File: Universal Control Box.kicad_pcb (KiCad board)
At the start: 2 copper layers, 169.7 x 93.2 mm, 84 parts, among them J101 Conn_01x06, J102 Conn_01x07, J103 USB_C_Receptacle_USB2.0, U101 ESP32-WROOM-32, U102 PCF8575DBR (PCF1), U103 AMS1117-3.3, U201 PEC11H-4025F-S0016, U202 PEC11H-4025F-S0016

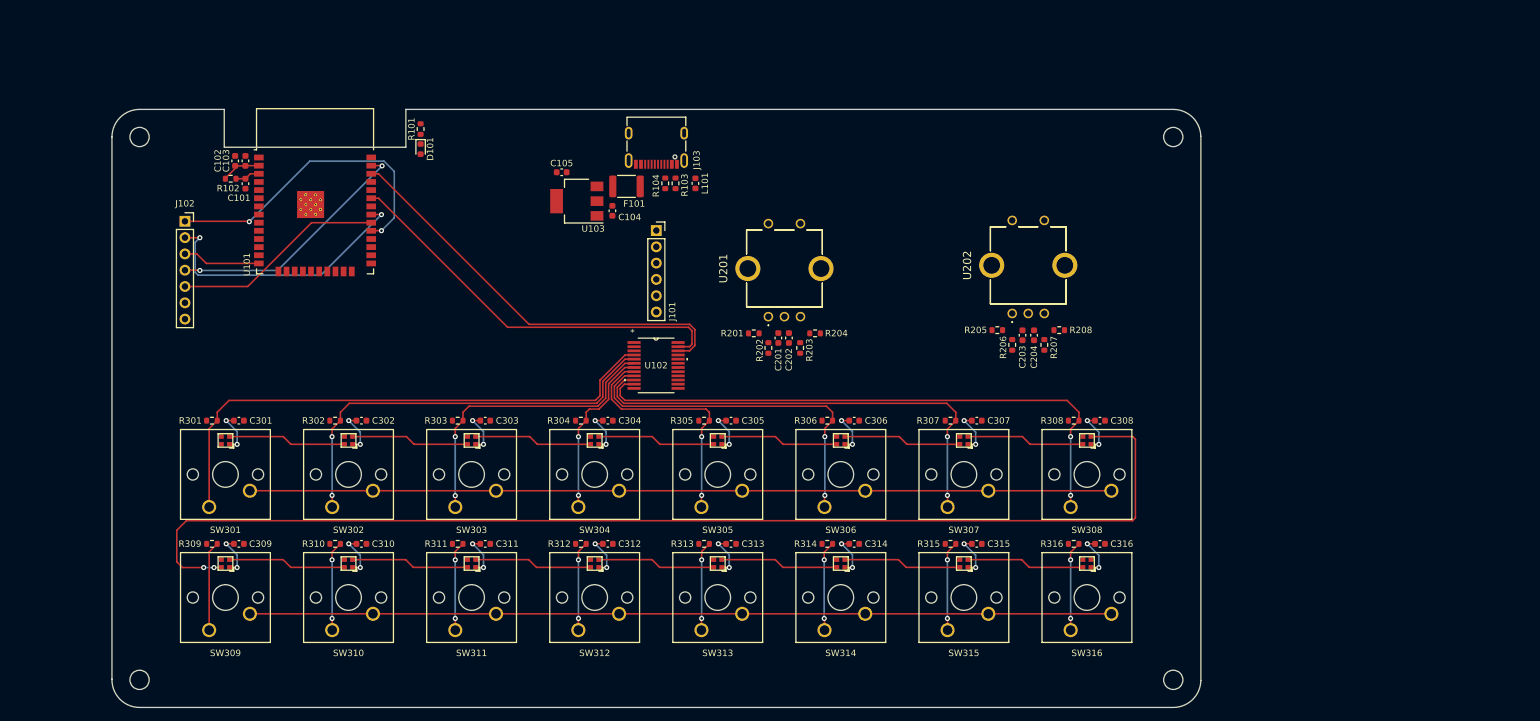
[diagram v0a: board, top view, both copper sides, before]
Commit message: Fixed LED Schematic & added 2 more LEDs
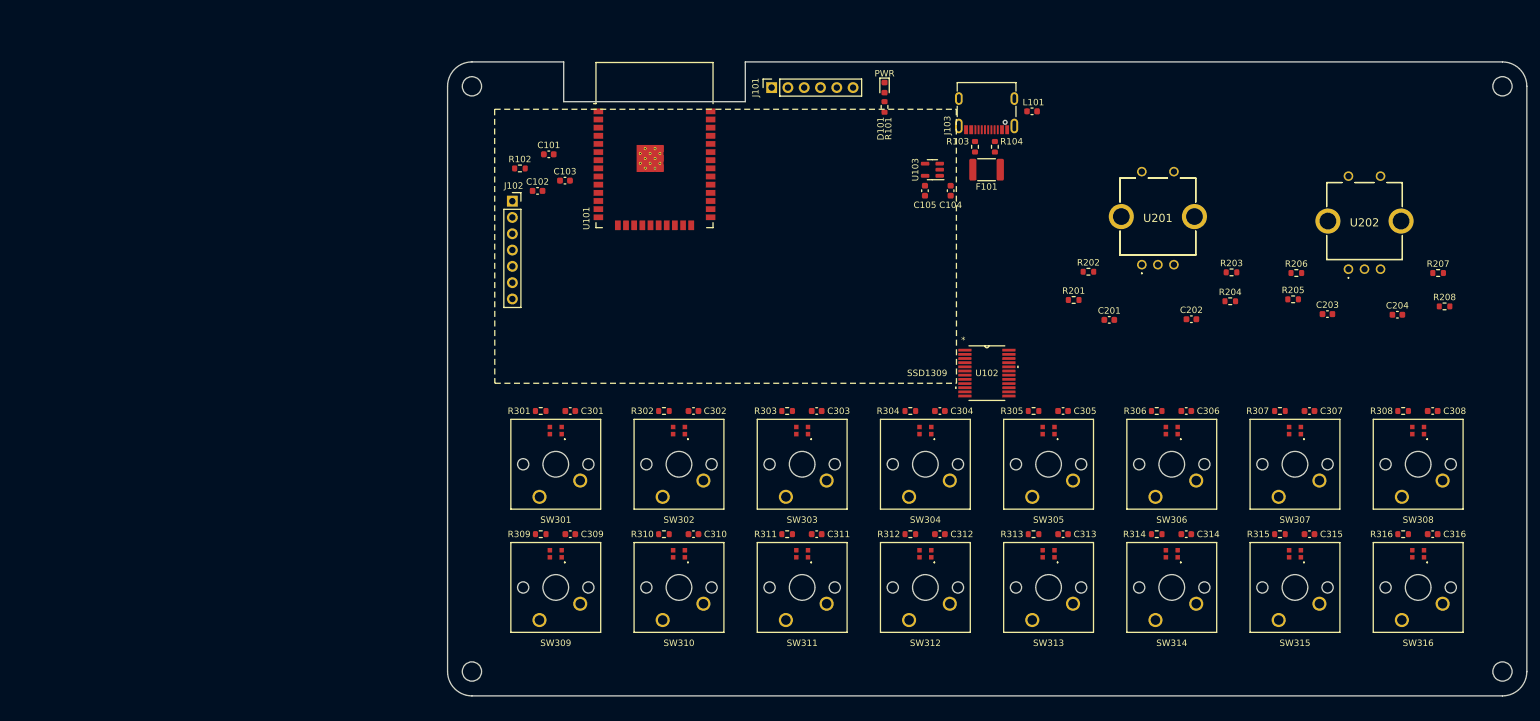
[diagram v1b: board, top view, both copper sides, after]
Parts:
- C104: value 10uF -> 22uF
- C105: value 10uF -> 4.7uF
- SW301, SW302, SW303, SW304, SW305, SW306, SW307, SW308, SW309, SW310, SW311, SW312, SW313, SW314, SW315, SW316: footprint Adam_Custom_Footprints:CherryMX_1.00u_PCB_SK6812-EC20 -> Adam_Custom_Footprints:CherryMX_1.00u_PCB_WS2812B-2020
- U103: value AMS1117-3.3 -> XC6220B331MR-G; footprint Package_TO_SOT_SMD:SOT-223-3_TabPin2 -> Package_TO_SOT_SMD:SOT-23-5
- moved H102 231.7 mm to (247.1, 30.7)
- moved H103 137.4 mm to (86.5, 121.9)
- moved D101 72.9 mm to (150.8, 30.9)
- moved R101 72.4 mm to (150.8, 33.9), turned to -90 degrees
- moved R203 68.2 mm to (204.9, 59.7), turned to 0 degrees
- moved R204 64.9 mm to (204.7, 64.2), turned to 0 degrees
- moved C202 62.8 mm to (198.6, 67.0), turned to 0 degrees
- moved R207 62.4 mm to (237.1, 59.8), turned to 0 degrees
- moved R208 60.2 mm to (238.1, 65.0), turned to 0 degrees
- moved U201 58.8 mm to (190.9, 58.5)
- moved C204 56.7 mm to (230.7, 66.3), turned to 0 degrees
- moved C105 56.7 mm to (157.1, 47.0), turned to -90 degrees
- moved F101 56.2 mm to (166.7, 43.7)
- moved U103 55.6 mm to (158.3, 43.7)
- moved L101 53.6 mm to (173.8, 34.6), turned to 180 degrees
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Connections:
- net /OLED_CLK renamed /OLED_SCL
- net /OLED_MOSI_SDA renamed /OLED_MOSI
- C104 pad 1: +5V -> GND
- C104 pad 2: GND -> +5V
- J102 pad 2: /OLED_MISO_SCK -> /OLED_DC
- SW301 pad 2: +5V -> /KeyCaps/SW1
- SW301 pad 3: Net-(SW301-DOUT) -> +5V
- SW301 pad 4: /KeyCaps/SW1 -> Net-(SW301-DOUT)
- SW302 pad 2: +5V -> /KeyCaps/SW2
- SW302 pad 3: Net-(SW302-DOUT) -> +5V
- SW302 pad 4: /KeyCaps/SW2 -> Net-(SW302-DOUT)
- SW303 pad 2: +5V -> /KeyCaps/SW3
- SW303 pad 3: Net-(SW303-DOUT) -> +5V
- SW303 pad 4: /KeyCaps/SW3 -> Net-(SW303-DOUT)
- SW304 pad 2: +5V -> /KeyCaps/SW4
- SW304 pad 3: Net-(SW304-DOUT) -> +5V
- SW304 pad 4: /KeyCaps/SW4 -> Net-(SW304-DOUT)
- SW305 pad 2: +5V -> /KeyCaps/SW5
- SW305 pad 3: Net-(SW305-DOUT) -> +5V
- SW305 pad 4: /KeyCaps/SW5 -> Net-(SW305-DOUT)
- SW306 pad 2: +5V -> /KeyCaps/SW6
- SW306 pad 3: Net-(SW306-DOUT) -> +5V
- SW306 pad 4: /KeyCaps/SW6 -> Net-(SW306-DOUT)
- SW307 pad 2: +5V -> /KeyCaps/SW7
- SW307 pad 3: Net-(SW307-DOUT) -> +5V
- SW307 pad 4: /KeyCaps/SW7 -> Net-(SW307-DOUT)
- SW308 pad 2: +5V -> /KeyCaps/SW8
- SW308 pad 3: Net-(SW308-DOUT) -> +5V
- SW308 pad 4: /KeyCaps/SW8 -> Net-(SW308-DOUT)
- SW309 pad 2: +5V -> /KeyCaps/SW9
- SW309 pad 3: Net-(SW309-DOUT) -> +5V
- SW309 pad 4: /KeyCaps/SW9 -> Net-(SW309-DOUT)
- SW310 pad 2: +5V -> /KeyCaps/SW10
- SW310 pad 3: Net-(SW310-DOUT) -> +5V
- SW310 pad 4: /KeyCaps/SW10 -> Net-(SW310-DOUT)
- SW311 pad 2: +5V -> /KeyCaps/SW11
- SW311 pad 3: Net-(SW311-DOUT) -> +5V
- SW311 pad 4: /KeyCaps/SW11 -> Net-(SW311-DOUT)
- SW312 pad 2: +5V -> /KeyCaps/SW12
- SW312 pad 3: Net-(SW312-DOUT) -> +5V
- SW312 pad 4: /KeyCaps/SW12 -> Net-(SW312-DOUT)
- SW313 pad 2: +5V -> /KeyCaps/SW13
- SW313 pad 3: Net-(SW313-DOUT) -> +5V
- SW313 pad 4: /KeyCaps/SW13 -> Net-(SW313-DOUT)
- SW314 pad 2: +5V -> /KeyCaps/SW14
- SW314 pad 3: Net-(SW314-DOUT) -> +5V
- SW314 pad 4: /KeyCaps/SW14 -> Net-(SW314-DOUT)
- SW315 pad 2: +5V -> /KeyCaps/SW15
- SW315 pad 3: Net-(SW315-DOUT) -> +5V
- SW315 pad 4: /KeyCaps/SW15 -> Net-(SW315-DOUT)
- SW316 pad 2: +5V -> /KeyCaps/SW16
- SW316 pad 3: unconnected-(SW316-DOUT-Pad3) -> +5V
- SW316 pad 4: /KeyCaps/SW16 -> unconnected-(SW316-DOUT-Pad4)
- U101 pad 14: /OLED_RESET -> unconnected-(U101-IO12-Pad14)
- U101 pad 31: /OLED_MISO_SCK -> /IO_INT
- U101 pad 8: unconnected-(U101-IO32-Pad8) -> /OLED_RESET
- U101 pad 9: unconnected-(U101-IO33-Pad9) -> /OLED_DC
- U102 pad 1: unconnected-(U102-*INT-Pad1) -> /IO_INT
- U102 pad 10: /KeyCaps/SW7 -> /KeyCaps/SW10
- U102 pad 11: /KeyCaps/SW8 -> /KeyCaps/SW9
- U102 pad 17: /KeyCaps/SW12 -> /KeyCaps/SW5
- U102 pad 18: /KeyCaps/SW11 -> /KeyCaps/SW6
- U102 pad 19: /KeyCaps/SW10 -> /KeyCaps/SW7
- U102 pad 20: /KeyCaps/SW9 -> /KeyCaps/SW8
- U102 pad 8: /KeyCaps/SW5 -> /KeyCaps/SW12
- U102 pad 9: /KeyCaps/SW6 -> /KeyCaps/SW11
- U103 pad 1: GND -> +5V
- U103 pad 2: +3.3V -> GND
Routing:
- net +3.3V: track 274.9 -> 0.00 mm
- net Net-(SW308-DOUT): track 181.8 -> 0.00 mm, vias 2 -> 0
- net +5V: track 109.1 -> 0.00 mm, vias 32 -> 0
- net /KeyCaps/SW8: track 91.4 -> 0.00 mm, vias 2 -> 0
- net /KeyCaps/SW1: track 85.4 -> 0.00 mm
- net /KeyCaps/SW7: track 73.6 -> 0.00 mm, vias 2 -> 0
- net /KeyCaps/SW2: track 66.0 -> 0.00 mm, vias 2 -> 0
- net /I2C_SCL: track 65.9 -> 0.00 mm
- net /I2C_SDA: track 63.0 -> 0.00 mm
- net /KeyCaps/SW6: track 55.8 -> 0.00 mm, vias 2 -> 0
- net /OLED_CS: track 48.9 -> 0.00 mm, vias 2 -> 0
- net /KeyCaps/SW3: track 46.5 -> 0.00 mm, vias 2 -> 0
- net /OLED_MISO_SCK: track 42.7 -> 0.00 mm, vias 2 -> 0
- net /OLED_MOSI: track 39.2 -> 0.00 mm, vias 2 -> 0
- net /KeyCaps/SW5: track 38.0 -> 0.00 mm, vias 2 -> 0
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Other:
- board size 169.7 x 93.2 mm -> 168.2 x 98.8 mm
- board text added: "PWR"

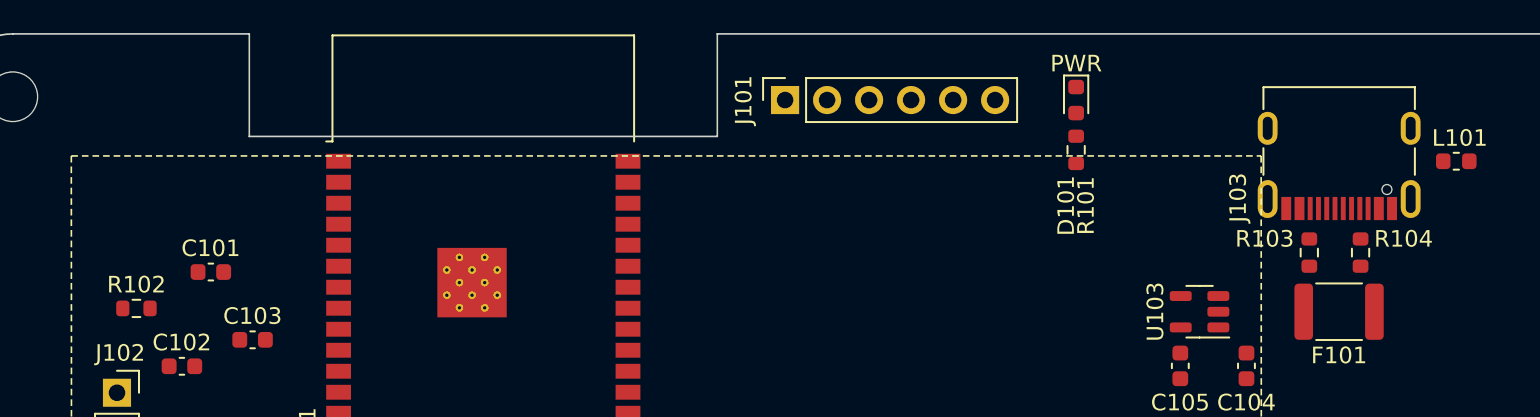
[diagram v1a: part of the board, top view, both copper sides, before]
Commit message: Added missing resistor for Green LED
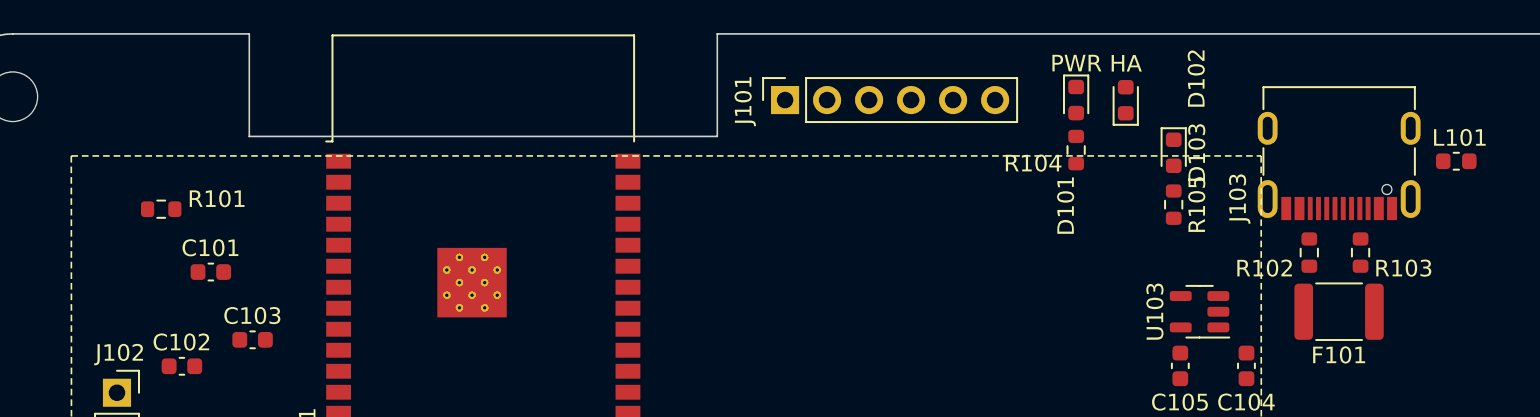
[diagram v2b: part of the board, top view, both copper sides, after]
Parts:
- added D102: Green, LED_SMD:LED_0603_1608Metric, F.Cu at (153.8, 30.9)
- added D103: Yellow, LED_SMD:LED_0603_1608Metric, F.Cu at (156.7, 34.1)
- added R105: 1K, Resistor_SMD:R_0603_1608Metric, F.Cu at (156.7, 37.2)
- R101: value 1K -> 10K
- R102: value 10K -> 5.1K
- R104: value 5.1K -> 1K
- moved R102 71.0 mm to (164.9, 40.1), turned to -90 degrees
- moved R101 55.4 mm to (95.5, 37.5), turned to 0 degrees
- moved R104 18.3 mm to (150.8, 33.9), turned to -90 degrees
- moved R103 3.10 mm to (168.0, 40.1), turned to 90 degrees
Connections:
- D101 pad 1: Net-(D101-K) -> GND
- D101 pad 2: +3.3V -> Net-(D101-A)
- R101 pad 1: Net-(D101-K) -> +3.3V
- R101 pad 2: GND -> /EN
- R102 pad 1: +3.3V -> Net-(J103-CC2)
- R102 pad 2: /EN -> GND
- R103 pad 1: Net-(J103-CC2) -> GND
- R103 pad 2: GND -> Net-(J103-CC1)
- R104 pad 1: GND -> Net-(D101-A)
- R104 pad 2: Net-(J103-CC1) -> +3.3V
- R302 pad 1: /KeyCaps/SW2 -> /KeyCaps/SW9
- R303 pad 1: /KeyCaps/SW3 -> /KeyCaps/SW2
- R304 pad 1: /KeyCaps/SW4 -> /KeyCaps/SW10
- R305 pad 1: /KeyCaps/SW5 -> /KeyCaps/SW3
- R306 pad 1: /KeyCaps/SW6 -> /KeyCaps/SW11
- R307 pad 1: /KeyCaps/SW7 -> /KeyCaps/SW4
- R308 pad 1: /KeyCaps/SW8 -> /KeyCaps/SW12
- R309 pad 1: /KeyCaps/SW9 -> /KeyCaps/SW5
- R310 pad 1: /KeyCaps/SW10 -> /KeyCaps/SW13
- R311 pad 1: /KeyCaps/SW11 -> /KeyCaps/SW6
- R312 pad 1: /KeyCaps/SW12 -> /KeyCaps/SW14
- R313 pad 1: /KeyCaps/SW13 -> /KeyCaps/SW7
- R314 pad 1: /KeyCaps/SW14 -> /KeyCaps/SW15
- R315 pad 1: /KeyCaps/SW15 -> /KeyCaps/SW8
- SW302 pad 2: /KeyCaps/SW2 -> /KeyCaps/SW9
- SW302 pad 5: Net-(SW301-DOUT) -> Net-(SW302-DIN)
- SW303 pad 2: /KeyCaps/SW3 -> /KeyCaps/SW2
- SW303 pad 5: Net-(SW302-DOUT) -> Net-(SW301-DOUT)
- SW304 pad 2: /KeyCaps/SW4 -> /KeyCaps/SW10
- SW304 pad 5: Net-(SW303-DOUT) -> Net-(SW302-DOUT)
- SW305 pad 2: /KeyCaps/SW5 -> /KeyCaps/SW3
- SW305 pad 5: Net-(SW304-DOUT) -> Net-(SW303-DOUT)
- SW306 pad 2: /KeyCaps/SW6 -> /KeyCaps/SW11
- SW306 pad 5: Net-(SW305-DOUT) -> Net-(SW304-DOUT)
- SW307 pad 2: /KeyCaps/SW7 -> /KeyCaps/SW4
- SW307 pad 5: Net-(SW306-DOUT) -> Net-(SW305-DOUT)
- SW308 pad 2: /KeyCaps/SW8 -> /KeyCaps/SW12
- SW308 pad 5: Net-(SW307-DOUT) -> Net-(SW306-DOUT)
- SW309 pad 2: /KeyCaps/SW9 -> /KeyCaps/SW5
- SW309 pad 5: Net-(SW308-DOUT) -> Net-(SW307-DOUT)
- SW310 pad 2: /KeyCaps/SW10 -> /KeyCaps/SW13
- SW310 pad 5: Net-(SW309-DOUT) -> Net-(SW308-DOUT)
- SW311 pad 2: /KeyCaps/SW11 -> /KeyCaps/SW6
- SW311 pad 5: Net-(SW310-DOUT) -> Net-(SW309-DOUT)
- SW312 pad 2: /KeyCaps/SW12 -> /KeyCaps/SW14
- SW312 pad 5: Net-(SW311-DOUT) -> Net-(SW310-DOUT)
- SW313 pad 2: /KeyCaps/SW13 -> /KeyCaps/SW7
- SW313 pad 5: Net-(SW312-DOUT) -> Net-(SW311-DOUT)
- SW314 pad 2: /KeyCaps/SW14 -> /KeyCaps/SW15
- SW314 pad 5: Net-(SW313-DOUT) -> Net-(SW312-DOUT)
- SW315 pad 2: /KeyCaps/SW15 -> /KeyCaps/SW8
- SW315 pad 4: Net-(SW315-DOUT) -> Net-(SW302-DIN)
- SW315 pad 5: Net-(SW314-DOUT) -> Net-(SW313-DOUT)
- SW316 pad 5: Net-(SW315-DOUT) -> Net-(SW314-DOUT)
- U101 pad 23: unconnected-(U101-IO15-Pad23) -> /HA_STATUS
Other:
- board text added: "HA"

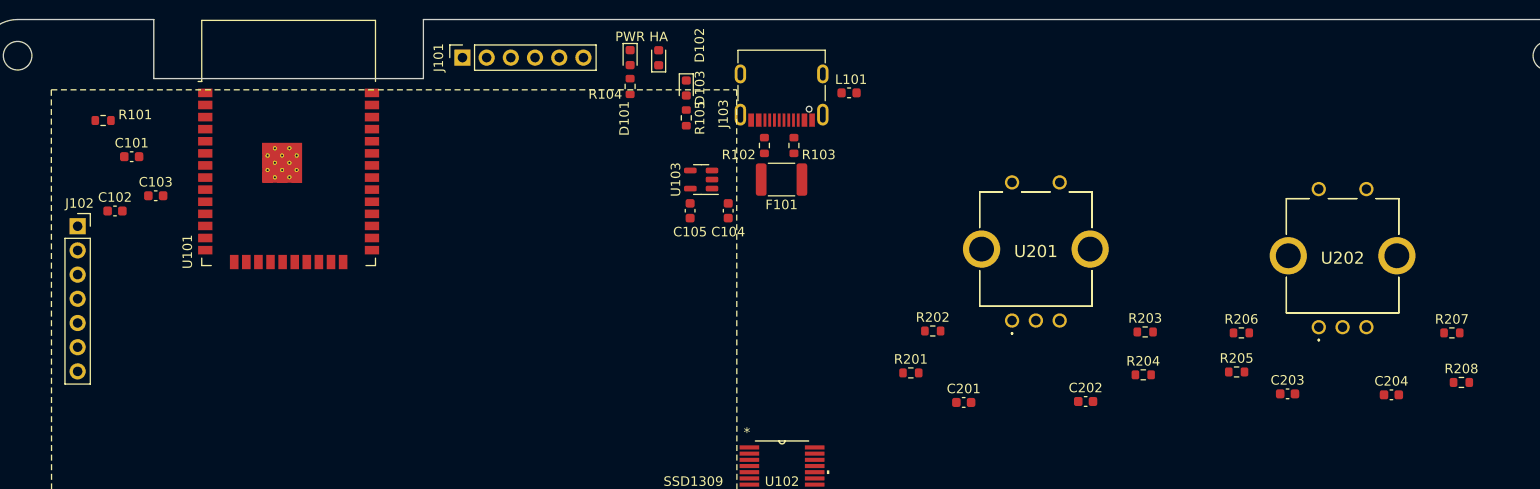
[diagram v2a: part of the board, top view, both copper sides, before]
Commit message: Updated PCB layout (no wires yet)
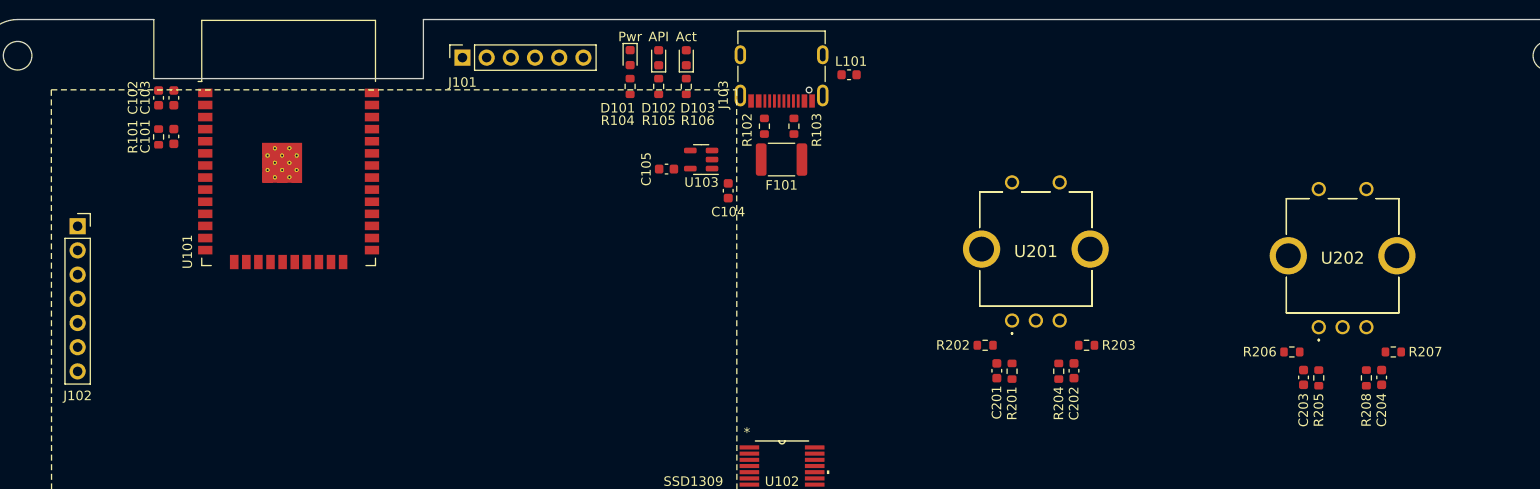
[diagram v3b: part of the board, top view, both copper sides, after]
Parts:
- added R106: 1K, Resistor_SMD:R_0603_1608Metric, F.Cu at (156.7, 33.9)
- moved C102 12.7 mm to (101.3, 35.1), turned to -90 degrees
- moved R201 10.6 mm to (190.9, 63.8), turned to -90 degrees
- moved C103 10.4 mm to (102.9, 35.1), turned to 90 degrees
- moved R208 9.99 mm to (228.1, 64.5), turned to 90 degrees
- moved R204 8.88 mm to (195.8, 63.8), turned to 90 degrees
- moved R205 8.65 mm to (223.1, 64.5), turned to -90 degrees
- moved R207 6.47 mm to (230.9, 61.8), turned to 180 degrees
- moved R203 6.31 mm to (198.7, 61.1), turned to 180 degrees
- moved R101 6.08 mm to (101.3, 39.2), turned to 90 degrees
- moved R202 5.70 mm to (188.1, 61.1)
- moved R206 5.66 mm to (220.3, 61.8)
- moved C105 5.03 mm to (154.6, 42.6), turned to 180 degrees
- moved C101 4.91 mm to (102.9, 39.2), turned to -90 degrees
- moved C201 4.81 mm to (189.3, 63.8), turned to -90 degrees
- moved R105 4.39 mm to (153.8, 33.9), turned to 90 degrees
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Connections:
- D102 pad 1: GND -> Net-(D102-K)
- R105 pad 1: Net-(D103-A) -> GND
- R105 pad 2: +3.3V -> Net-(D102-K)
- R302 pad 1: /KeyCaps/SW9 -> /KeyCaps/SW2
- R303 pad 1: /KeyCaps/SW2 -> /KeyCaps/SW3
- R304 pad 1: /KeyCaps/SW10 -> /KeyCaps/SW4
- R305 pad 1: /KeyCaps/SW3 -> /KeyCaps/SW5
- R306 pad 1: /KeyCaps/SW11 -> /KeyCaps/SW6
- R307 pad 1: /KeyCaps/SW4 -> /KeyCaps/SW7
- R308 pad 1: /KeyCaps/SW12 -> /KeyCaps/SW8
- R309 pad 1: /KeyCaps/SW5 -> /KeyCaps/SW9
- R310 pad 1: /KeyCaps/SW13 -> /KeyCaps/SW10
- R311 pad 1: /KeyCaps/SW6 -> /KeyCaps/SW11
- R312 pad 1: /KeyCaps/SW14 -> /KeyCaps/SW12
- R313 pad 1: /KeyCaps/SW7 -> /KeyCaps/SW13
- R314 pad 1: /KeyCaps/SW15 -> /KeyCaps/SW14
- R315 pad 1: /KeyCaps/SW8 -> /KeyCaps/SW15
- SW302 pad 2: /KeyCaps/SW9 -> /KeyCaps/SW2
- SW302 pad 5: Net-(SW302-DIN) -> Net-(SW301-DOUT)
- SW303 pad 2: /KeyCaps/SW2 -> /KeyCaps/SW3
- SW303 pad 5: Net-(SW301-DOUT) -> Net-(SW302-DOUT)
- SW304 pad 2: /KeyCaps/SW10 -> /KeyCaps/SW4
- SW304 pad 5: Net-(SW302-DOUT) -> Net-(SW303-DOUT)
- SW305 pad 2: /KeyCaps/SW3 -> /KeyCaps/SW5
- SW305 pad 5: Net-(SW303-DOUT) -> Net-(SW304-DOUT)
- SW306 pad 2: /KeyCaps/SW11 -> /KeyCaps/SW6
- SW306 pad 5: Net-(SW304-DOUT) -> Net-(SW305-DOUT)
- SW307 pad 2: /KeyCaps/SW4 -> /KeyCaps/SW7
- SW307 pad 5: Net-(SW305-DOUT) -> Net-(SW306-DOUT)
- SW308 pad 2: /KeyCaps/SW12 -> /KeyCaps/SW8
- SW308 pad 5: Net-(SW306-DOUT) -> Net-(SW307-DOUT)
- SW309 pad 2: /KeyCaps/SW5 -> /KeyCaps/SW9
- SW309 pad 5: Net-(SW307-DOUT) -> Net-(SW308-DOUT)
- SW310 pad 2: /KeyCaps/SW13 -> /KeyCaps/SW10
- SW310 pad 5: Net-(SW308-DOUT) -> Net-(SW309-DOUT)
- SW311 pad 2: /KeyCaps/SW6 -> /KeyCaps/SW11
- SW311 pad 5: Net-(SW309-DOUT) -> Net-(SW310-DOUT)
- SW312 pad 2: /KeyCaps/SW14 -> /KeyCaps/SW12
- SW312 pad 5: Net-(SW310-DOUT) -> Net-(SW311-DOUT)
- SW313 pad 2: /KeyCaps/SW7 -> /KeyCaps/SW13
- SW313 pad 5: Net-(SW311-DOUT) -> Net-(SW312-DOUT)
- SW314 pad 2: /KeyCaps/SW15 -> /KeyCaps/SW14
- SW314 pad 5: Net-(SW312-DOUT) -> Net-(SW313-DOUT)
- SW315 pad 2: /KeyCaps/SW8 -> /KeyCaps/SW15
- SW315 pad 4: Net-(SW302-DIN) -> Net-(SW315-DOUT)
- SW315 pad 5: Net-(SW313-DOUT) -> Net-(SW314-DOUT)
- SW316 pad 5: Net-(SW314-DOUT) -> Net-(SW315-DOUT)
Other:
- board text added: "API"
- board text added: "Act"
- board text added: "Pwr"
- board text removed: "HA"
- board text removed: "PWR"
